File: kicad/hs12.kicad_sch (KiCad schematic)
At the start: 8 parts, among them U1 12V, U3 12V, U4 12V

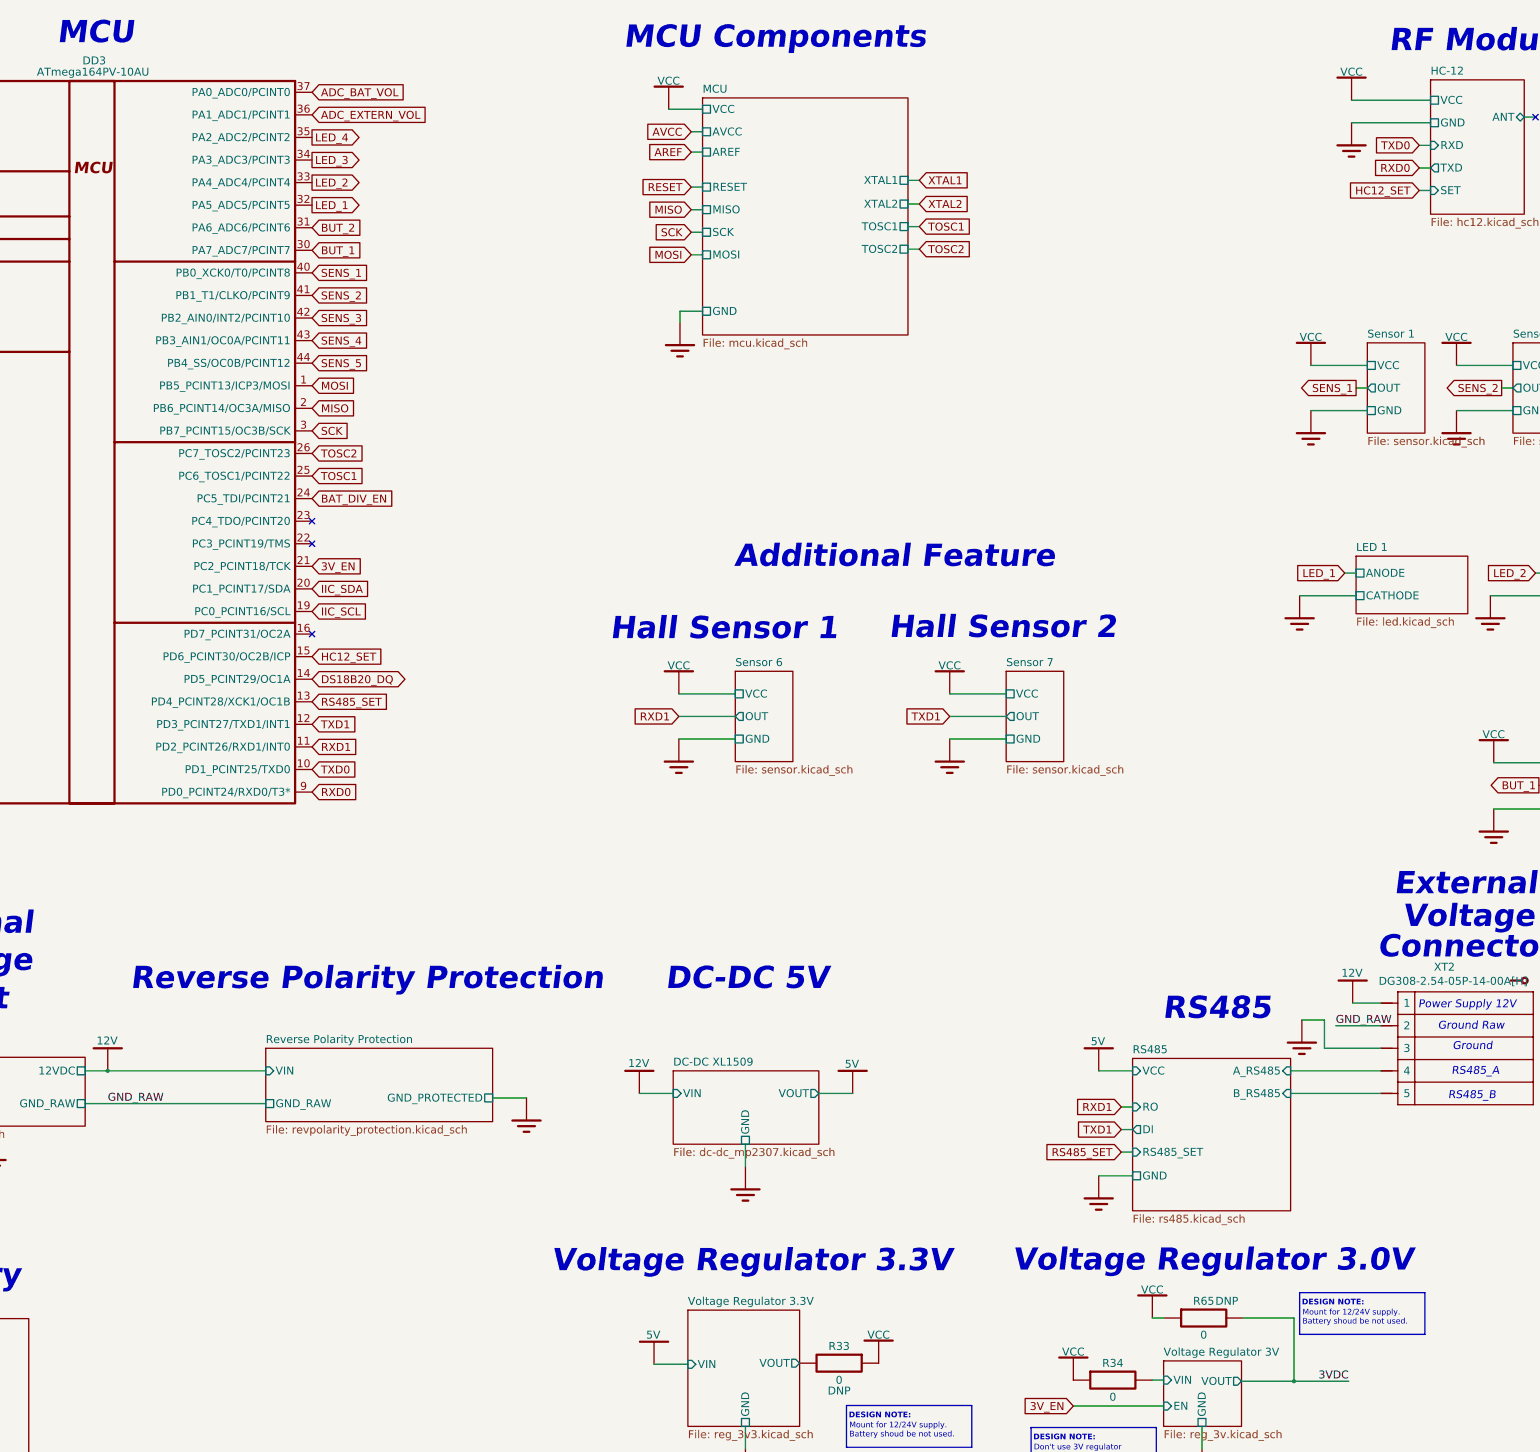
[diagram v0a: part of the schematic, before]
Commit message: Reannotate schematic; Fix 5032 crystal footprint field; Update PCB with 5032 crystal
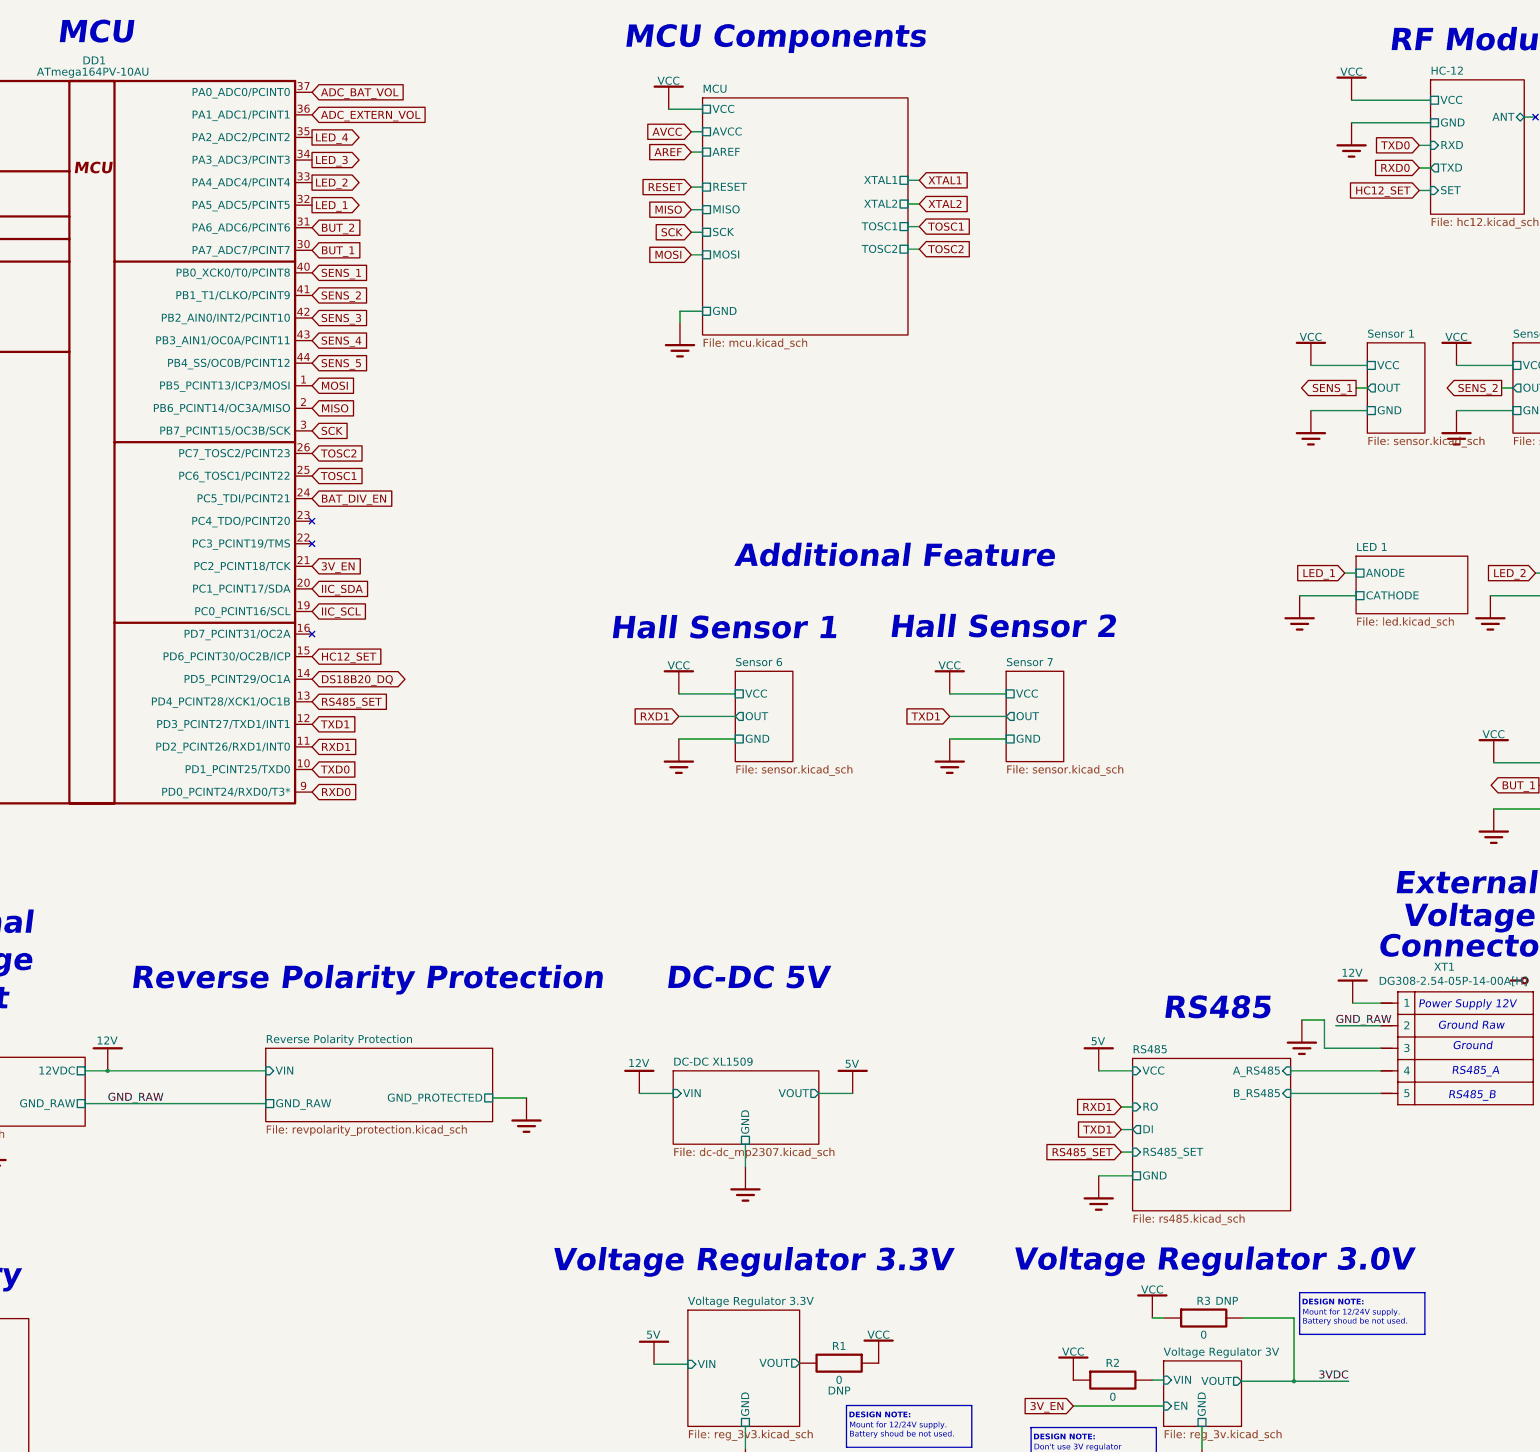
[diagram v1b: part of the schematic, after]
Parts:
- renumbered DD3 to DD1, R33 to R1, R34 to R2, R65 to R3, U4 to U2, XT2 to XT1
